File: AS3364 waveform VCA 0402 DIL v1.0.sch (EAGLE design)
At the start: 47 parts, among them IC1 TL072JD, IC2 TL072JD

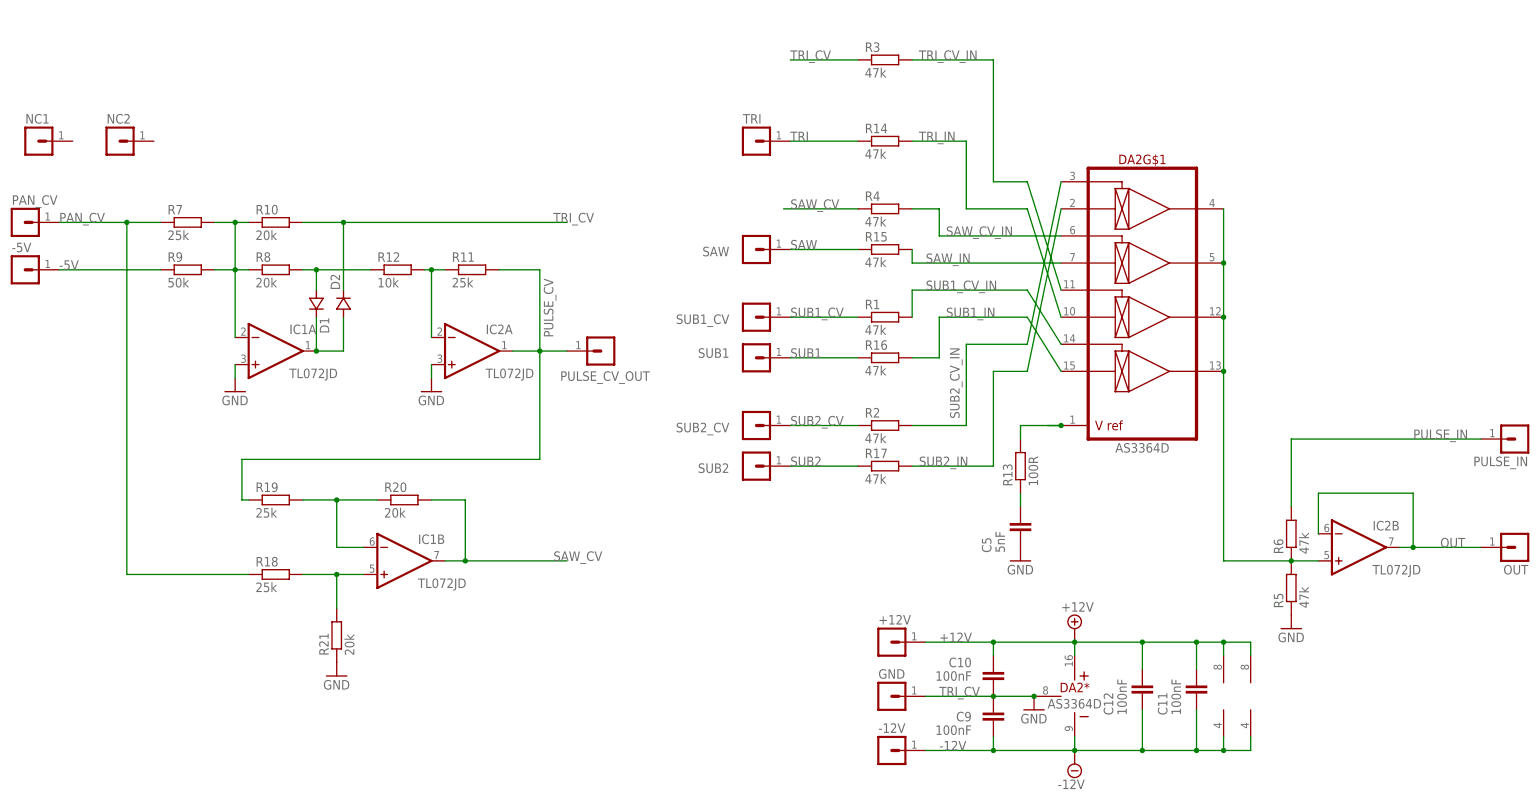
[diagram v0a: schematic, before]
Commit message: Finished waveshape mixer and fixed a serious bug
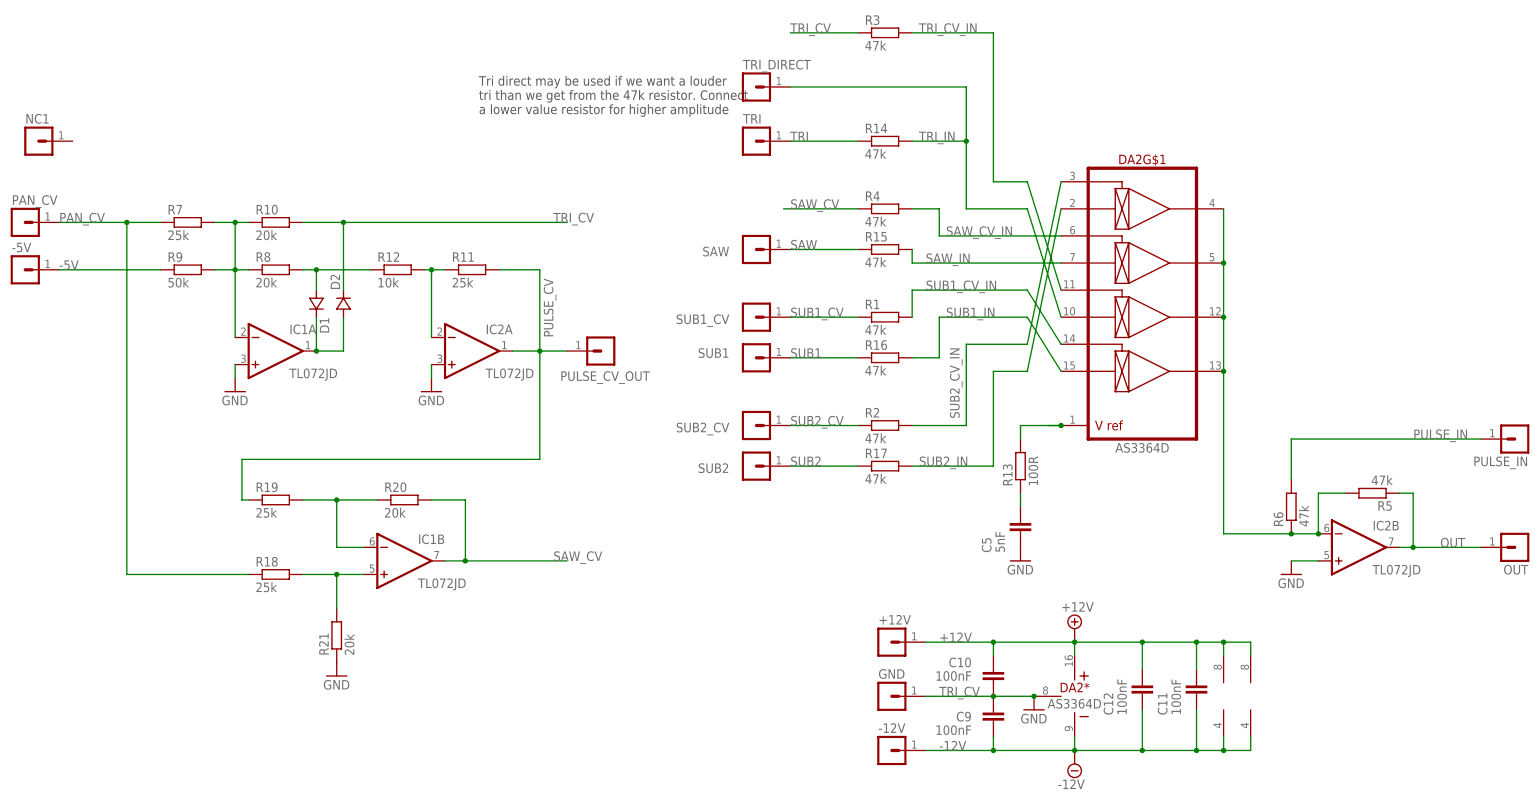
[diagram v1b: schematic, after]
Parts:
- removed NC2: (no value), joakim:MA01-1JP
- added TRI_DIRECT: (no value), joakim:MA01-1JP
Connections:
- net GND: now also IC2B.+IN; no longer R5.1
- net MIX_BUS: now also IC2B.-IN; no longer IC2B.+IN
- net OUT: now also R5.1; no longer IC2B.-IN
- net TRI_IN: now also TRI_DIRECT.1
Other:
- note added: "Tri direct may be used if we want a louder tri than we get from the 47k resistor. Connect a lower value resistor for higher amplitude"
- moved on the sheet: R3, R5, R6
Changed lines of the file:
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@@
 <setting verticaltext="up"/>
 </settings>
-<grid distance="0.05" unitdist="inch" unit="inch" style="lines" multiple="1" display="no" altdistance="0.01" altunitdist="inch" altunit="inch"/>
+<grid distance="0.1" unitdist="inch" unit="inch" style="lines" multiple="1" display="no" altdistance="0.01" altunitdist="inch" altunit="inch"/>
 <layers>
 <layer number="1" name="Top" color="4" fill="1" visible="no" active="no"/>
@@
 <part name="PAN_CV" library="joakim" deviceset="MA01-1J" device="P"/>
 <part name="NC1" library="joakim" deviceset="MA01-1J" device="P"/>
-<part name="NC2" library="joakim" deviceset="MA01-1J" device="P"/>
+<part name="TRI_DIRECT" library="joakim" deviceset="MA01-1J" device="P"/>
 </parts>
 <sheets>
 <sheet>
 <plain>
+<text x="-60.96" y="88.9" size="1.778" layer="97">Tri direct may be used if we want a louder
+tri than we get from the 47k resistor. Connect
+a lower value resistor for higher amplitude</text>
 </plain>
 <instances>
@@
 <attribute name="VALUE" x="11.43" y="27.178" size="1.778" layer="96"/>
 </instance>
-<instance part="R3" gate="G$1" x="15.24" y="99.06" smashed="yes">
-<attribute name="NAME" x="11.43" y="100.5586" size="1.778" layer="95"/>
-<attribute name="VALUE" x="11.43" y="95.758" size="1.778" layer="96"/>
+<instance part="R3" gate="G$1" x="15.24" y="104.14" smashed="yes">
+<attribute name="NAME" x="11.43" y="105.6386" size="1.778" layer="95"/>
+<attribute name="VALUE" x="11.43" y="100.838" size="1.778" layer="96"/>
 </instance>
 <instance part="R4" gate="G$1" x="15.24" y="71.12" smashed="yes">
@@
 <attribute name="VALUE" x="11.43" y="67.818" size="1.778" layer="96"/>
 </instance>
-<instance part="R5" gate="G$1" x="91.44" y="0" smashed="yes" rot="R90">
-<attribute name="NAME" x="89.9414" y="-3.81" size="1.778" layer="95" rot="R90"/>
-<attribute name="VALUE" x="94.742" y="-3.81" size="1.778" layer="96" rot="R90"/>
+<instance part="R5" gate="G$1" x="106.68" y="17.78" smashed="yes" rot="R180">
+<attribute name="NAME" x="110.49" y="16.2814" size="1.778" layer="95" rot="R180"/>
+<attribute name="VALUE" x="110.49" y="21.082" size="1.778" layer="96" rot="R180"/>
 </instance>
 <instance part="C9" gate="G$1" x="35.56" y="-25.4" smashed="yes" rot="R180">
@@
 <attribute name="VALUE" x="43.942" y="19.05" size="1.778" layer="96" rot="R90"/>
 </instance>
-<instance part="GND4" gate="1" x="91.44" y="-7.62" smashed="yes">
-<attribute name="VALUE" x="88.9" y="-10.16" size="1.778" layer="96"/>
+<instance part="GND4" gate="1" x="91.44" y="2.54" smashed="yes">
+<attribute name="VALUE" x="88.9" y="0" size="1.778" layer="96"/>
 </instance>
 <instance part="SUB1_CV" gate="G$1" x="-10.16" y="50.8" smashed="yes">
@@
 <attribute name="NAME" x="135.89" y="24.638" size="1.778" layer="95" rot="R180"/>
 </instance>
-<instance part="R6" gate="G$1" x="91.44" y="10.16" smashed="yes" rot="R90">
-<attribute name="NAME" x="89.9414" y="6.35" size="1.778" layer="95" rot="R90"/>
-<attribute name="VALUE" x="94.742" y="6.35" size="1.778" layer="96" rot="R90"/>
+<instance part="R6" gate="G$1" x="91.44" y="15.24" smashed="yes" rot="R90">
+<attribute name="NAME" x="89.9414" y="11.43" size="1.778" layer="95" rot="R90"/>
+<attribute name="VALUE" x="94.742" y="11.43" size="1.778" layer="96" rot="R90"/>
 </instance>
 <instance part="R7" gate="G$1" x="-115.57" y="68.58" smashed="yes">
@@
 <attribute name="NAME" x="-146.05" y="87.122" size="1.778" layer="95"/>
 </instance>
-<instance part="NC2" gate="G$1" x="-129.54" y="83.82" smashed="yes">
-<attribute name="VALUE" x="-130.81" y="78.74" size="1.778" layer="96"/>
-<attribute name="NAME" x="-130.81" y="87.122" size="1.778" layer="95"/>
+<instance part="TRI_DIRECT" gate="G$1" x="-10.16" y="93.98" smashed="yes">
+<attribute name="VALUE" x="-11.43" y="88.9" size="1.778" layer="96"/>
+<attribute name="NAME" x="-11.43" y="97.282" size="1.778" layer="95"/>
 </instance>
 </instances>
@@
 <pinref part="IC2" gate="B" pin="OUT"/>
 <label x="119.38" y="7.62" size="1.778" layer="95"/>
-<wire x1="96.52" y1="10.16" x2="96.52" y2="17.78" width="0.1524" layer="91"/>
-<pinref part="IC2" gate="B" pin="-IN"/>
-<wire x1="114.3" y1="17.78" x2="96.52" y2="17.78" width="0.1524" layer="91"/>
+<pinref part="R5" gate="G$1" pin="1"/>
+<wire x1="111.76" y1="17.78" x2="114.3" y2="17.78" width="0.1524" layer="91"/>
 </segment>
 </net>
@@
 </segment>
 <segment>
-<pinref part="R5" gate="G$1" pin="1"/>
-<pinref part="GND4" gate="1" pin="GND"/>
-</segment>
-<segment>
 <pinref part="IC2" gate="A" pin="+IN"/>
 <wire x1="-69.85" y1="41.91" x2="-69.85" y2="39.37" width="0.1524" layer="91"/>
@@
 <pinref part="GND2" gate="1" pin="GND"/>
 <wire x1="-106.68" y1="41.91" x2="-106.68" y2="39.37" width="0.1524" layer="91"/>
+</segment>
+<segment>
+<pinref part="IC2" gate="B" pin="+IN"/>
+<pinref part="GND4" gate="1" pin="GND"/>
+<wire x1="96.52" y1="5.08" x2="91.44" y2="5.08" width="0.1524" layer="91"/>
 </segment>
 </net>
@@
 <pinref part="DA2" gate="G$1" pin="IN3"/>
 <wire x1="41.91" y1="71.12" x2="48.26" y2="50.8" width="0.1524" layer="91"/>
+<pinref part="TRI_DIRECT" gate="G$1" pin="1"/>
+<wire x1="-2.54" y1="93.98" x2="30.48" y2="93.98" width="0.1524" layer="91"/>
+<wire x1="30.48" y1="93.98" x2="30.48" y2="83.82" width="0.1524" layer="91"/>
+<junction x="30.48" y="83.82"/>
 </segment>
 </net>
@@
 <segment>
 <pinref part="R3" gate="G$1" pin="2"/>
-<wire x1="35.56" y1="99.06" x2="35.56" y2="76.2" width="0.1524" layer="91"/>
+<wire x1="35.56" y1="104.14" x2="35.56" y2="76.2" width="0.1524" layer="91"/>
 <wire x1="35.56" y1="76.2" x2="41.91" y2="76.2" width="0.1524" layer="91"/>
-<wire x1="20.32" y1="99.06" x2="35.56" y2="99.06" width="0.1524" layer="91"/>
-<label x="21.59" y="99.06" size="1.778" layer="95"/>
+<wire x1="20.32" y1="104.14" x2="35.56" y2="104.14" width="0.1524" layer="91"/>
+<label x="21.59" y="104.14" size="1.778" layer="95"/>
 <pinref part="DA2" gate="G$1" pin="CV3"/>
 <wire x1="41.91" y1="76.2" x2="48.26" y2="55.88" width="0.1524" layer="91"/>
@@
 <segment>
 <pinref part="R6" gate="G$1" pin="2"/>
-<wire x1="91.44" y1="15.24" x2="91.44" y2="27.94" width="0.1524" layer="91"/>
+<wire x1="91.44" y1="20.32" x2="91.44" y2="27.94" width="0.1524" layer="91"/>
 <pinref part="PULSE_IN" gate="G$1" pin="1"/>
 <wire x1="91.44" y1="27.94" x2="127" y2="27.94" width="0.1524" layer="91"/>
@@
 <segment>
 <pinref part="R3" gate="G$1" pin="1"/>
-<wire x1="-2.54" y1="99.06" x2="10.16" y2="99.06" width="0.1524" layer="91"/>
+<wire x1="-2.54" y1="104.14" x2="10.16" y2="104.14" width="0.1524" layer="91"/>
 <label x="25.4" y="-20.32" size="1.778" layer="95"/>
-<label x="-2.54" y="99.06" size="1.778" layer="95"/>
+<label x="-2.54" y="104.14" size="1.778" layer="95"/>
 </segment>
 </net>
@@
 <wire x1="78.74" y1="60.96" x2="78.74" y2="50.8" width="0.1524" layer="91"/>
 <junction x="78.74" y="60.96"/>
-<pinref part="IC2" gate="B" pin="+IN"/>
-<pinref part="R5" gate="G$1" pin="2"/>
-<wire x1="96.52" y1="5.08" x2="91.44" y2="5.08" width="0.1524" layer="91"/>
-<wire x1="91.44" y1="5.08" x2="78.74" y2="5.08" width="0.1524" layer="91"/>
-<junction x="91.44" y="5.08"/>
-<wire x1="78.74" y1="40.64" x2="78.74" y2="5.08" width="0.1524" layer="91"/>
+<wire x1="78.74" y1="40.64" x2="78.74" y2="10.16" width="0.1524" layer="91"/>
 <pinref part="DA2" gate="G$1" pin="OUT4"/>
-<pinref part="R6" gate="G$1" pin="1"/>
 <wire x1="78.74" y1="50.8" x2="78.74" y2="40.64" width="0.1524" layer="91"/>
 <junction x="78.74" y="50.8"/>
 <junction x="78.74" y="40.64"/>
+<pinref part="R6" gate="G$1" pin="1"/>
+<wire x1="78.74" y1="10.16" x2="91.44" y2="10.16" width="0.1524" layer="91"/>
+<wire x1="96.52" y1="10.16" x2="96.52" y2="17.78" width="0.1524" layer="91"/>
+<pinref part="IC2" gate="B" pin="-IN"/>
+<wire x1="96.52" y1="10.16" x2="91.44" y2="10.16" width="0.1524" layer="91"/>
+<junction x="96.52" y="10.16"/>
+<junction x="91.44" y="10.16"/>
+<pinref part="R5" gate="G$1" pin="2"/>
+<wire x1="96.52" y1="17.78" x2="101.6" y2="17.78" width="0.1524" layer="91"/>
 </segment>
 </net>
@@
 </drawing>
 <compatibility>
+<note version="6.3" minversion="6.2.2" severity="warning">
+Since Version 6.2.2 text objects can contain more than one line,
+which will not be processed correctly with this version.
+</note>
 <note version="8.2" severity="warning">
 Since Version 8.2, EAGLE supports online libraries. The ids
